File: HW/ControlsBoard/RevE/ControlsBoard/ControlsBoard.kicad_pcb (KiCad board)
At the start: 2 copper layers, 54.6 x 29.8 mm, 12 parts, among them J1 Conn_02x06_Odd_Even, SW1 Rotary_Encoder_Switch, SW2 SW_SPST, SW3 SW_SPST, SW4 SW_SPST, SW5 SW_SPST

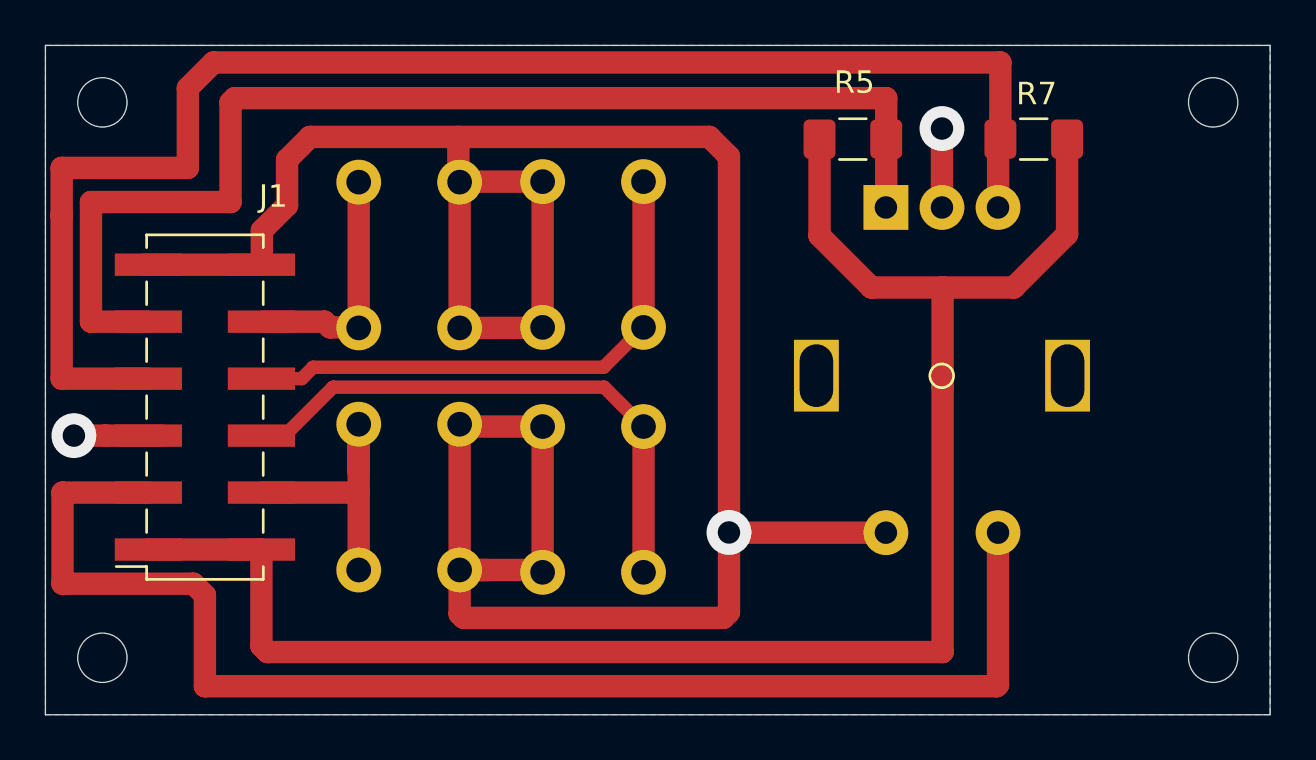
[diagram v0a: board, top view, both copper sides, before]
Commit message: updated front panel svg
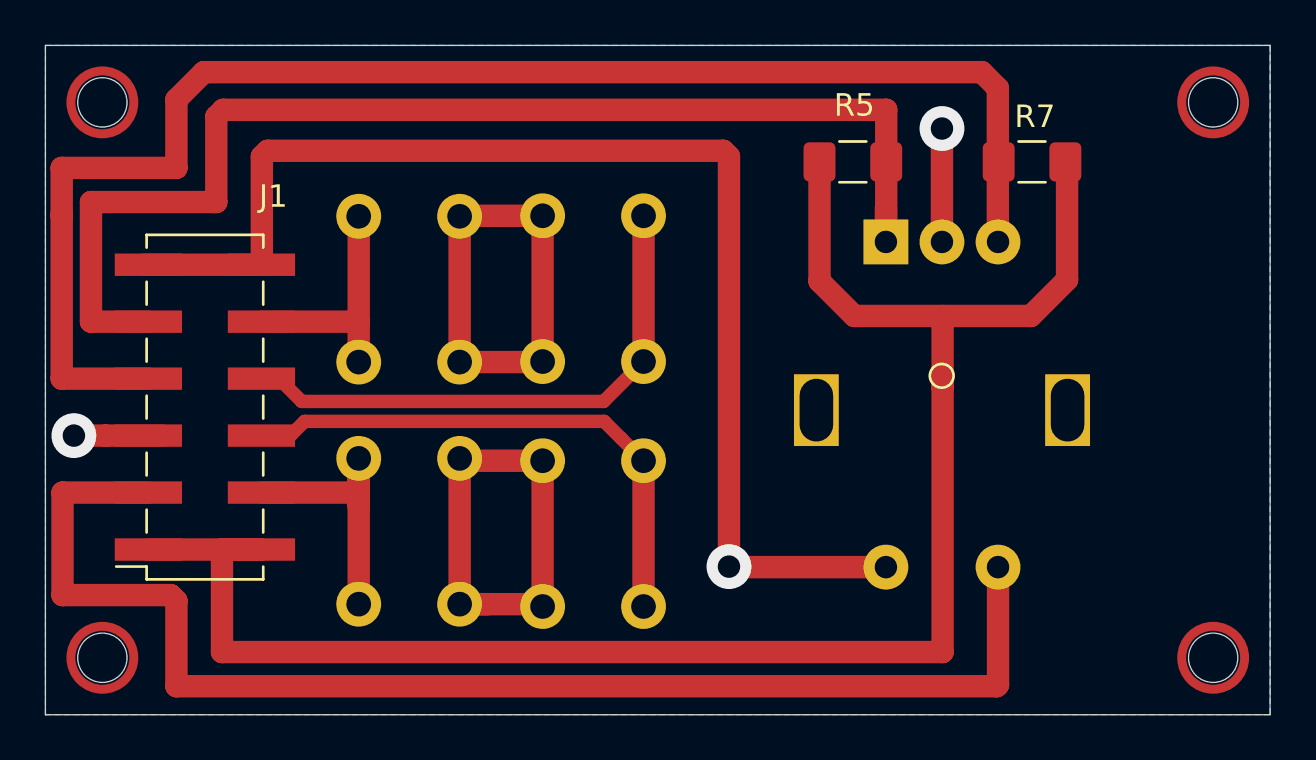
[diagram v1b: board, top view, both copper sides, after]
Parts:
- moved SW1 1.54 mm to (151.8, 51.3)
- moved SW2 1.52 mm to (128.3, 61.0)
- moved SW4 1.52 mm to (141.0, 56.6)
- moved SW5 1.52 mm to (128.3, 50.2)
- moved SW3 1.52 mm to (141.0, 67.6)
- moved R7 1.02 mm to (158.3, 47.7)
- moved R5 1.02 mm to (150.3, 47.7)
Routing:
- net GNDS: track 124.1 -> 107.7 mm
- net +3V3: track 77.6 -> 81.4 mm
- net /Controls/ENC_A: track 52.8 -> 54.7 mm
- net /Controls/ENC_SW: track 60.7 -> 59.3 mm
- net /Controls/BTN2: track 25.2 -> 24.5 mm
